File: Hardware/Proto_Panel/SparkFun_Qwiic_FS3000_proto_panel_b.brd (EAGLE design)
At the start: 69.8 x 103.6 mm, 327 parts, among them J11 QWIIC_RA, J12 QWIIC_RA, J15 QWIIC_RA, J18 QWIIC_RA, J19 QWIIC_RA, J2 QWIIC_RA, J3 QWIIC_RA, J4 QWIIC_RA, J8 QWIIC_RA, U1 FS3000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

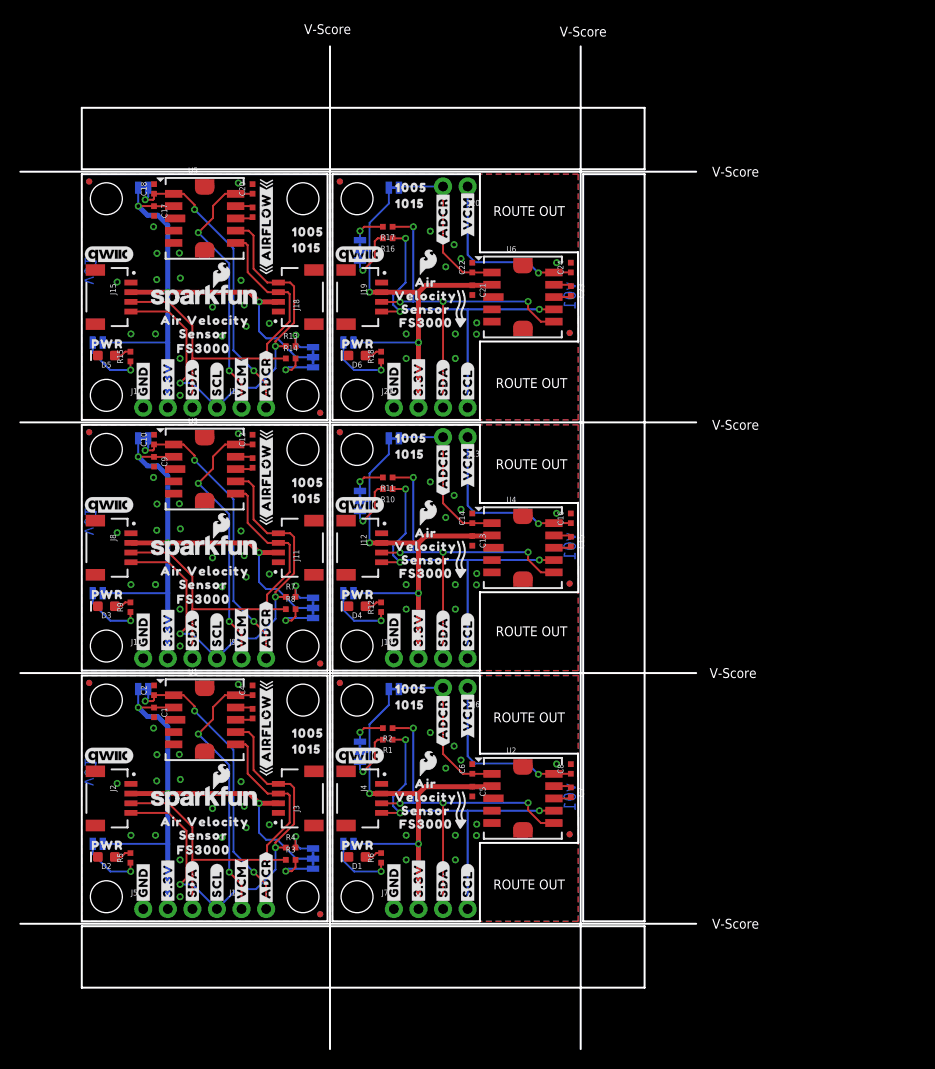
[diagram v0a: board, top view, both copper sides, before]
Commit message: re-panelized proto to meet 70cm width requirement for V-Scores
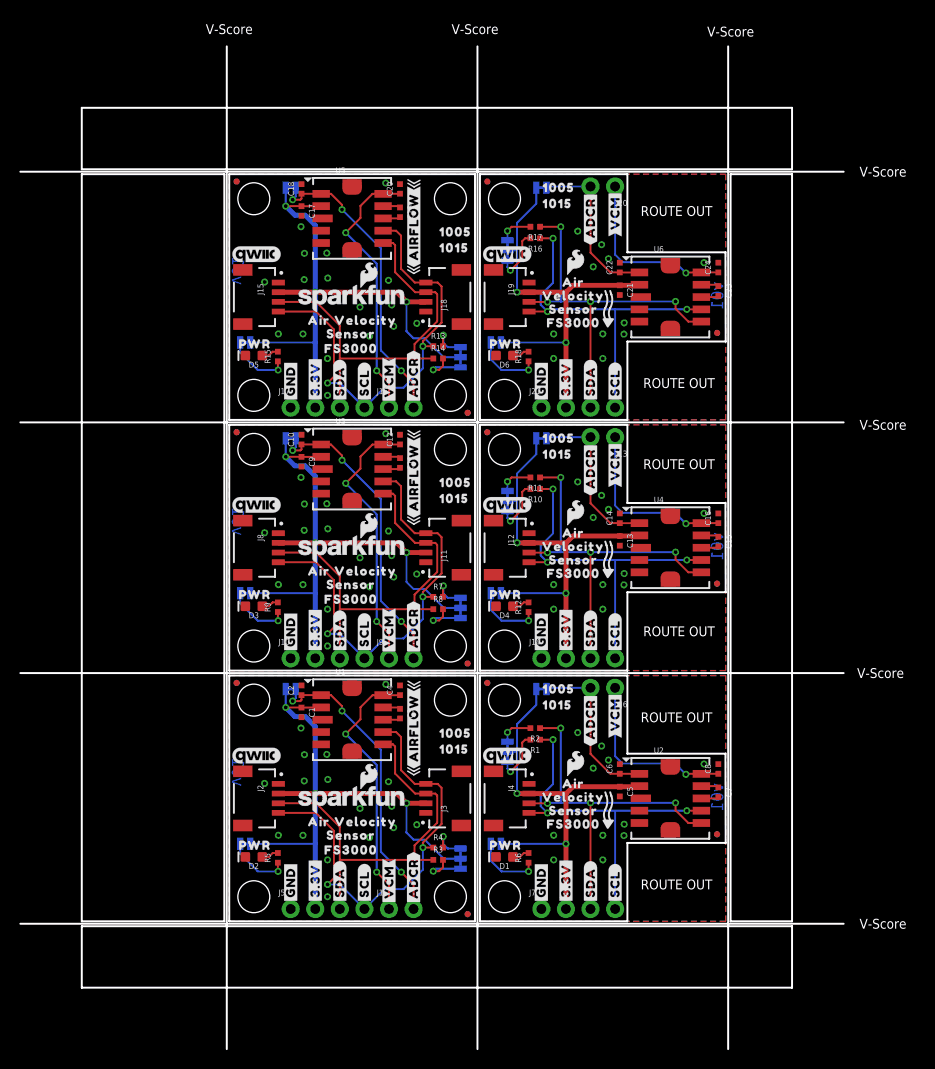
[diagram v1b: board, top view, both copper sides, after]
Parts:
- moved JP10 15.2 mm to (65.7, 15.8)
- moved JP13 15.2 mm to (65.7, 15.8)
- moved JP27 15.2 mm to (65.7, 41.8)
- moved JP29 15.2 mm to (65.7, 41.8)
- moved JP43 15.2 mm to (65.7, 67.7)
- moved JP45 15.2 mm to (65.7, 67.7)
- moved C11 15.2 mm to (32.9, 54.2)
- moved C12 15.2 mm to (32.9, 56.6)
- moved C13 15.2 mm to (55.6, 46.2)
- moved C14 15.2 mm to (55.6, 48.5)
- moved C15 15.2 mm to (65.8, 46.1)
- moved C16 15.2 mm to (65.8, 48.5)
- moved C19 15.2 mm to (32.9, 80.1)
- moved C20 15.2 mm to (32.9, 82.5)
- moved C21 15.2 mm to (55.6, 72.1)
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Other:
- board size 69.8 x 103.6 mm -> 85.1 x 103.6 mm
